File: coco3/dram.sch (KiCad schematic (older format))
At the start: 11 parts, among them CN4 Conn_01x12_Female, CN5 Conn_01x12_Female, CN6 Conn_01x12_Female, IC16 TMS4464, IC17 TMS4464, IC18 TMS4464, IC19 TMS4464

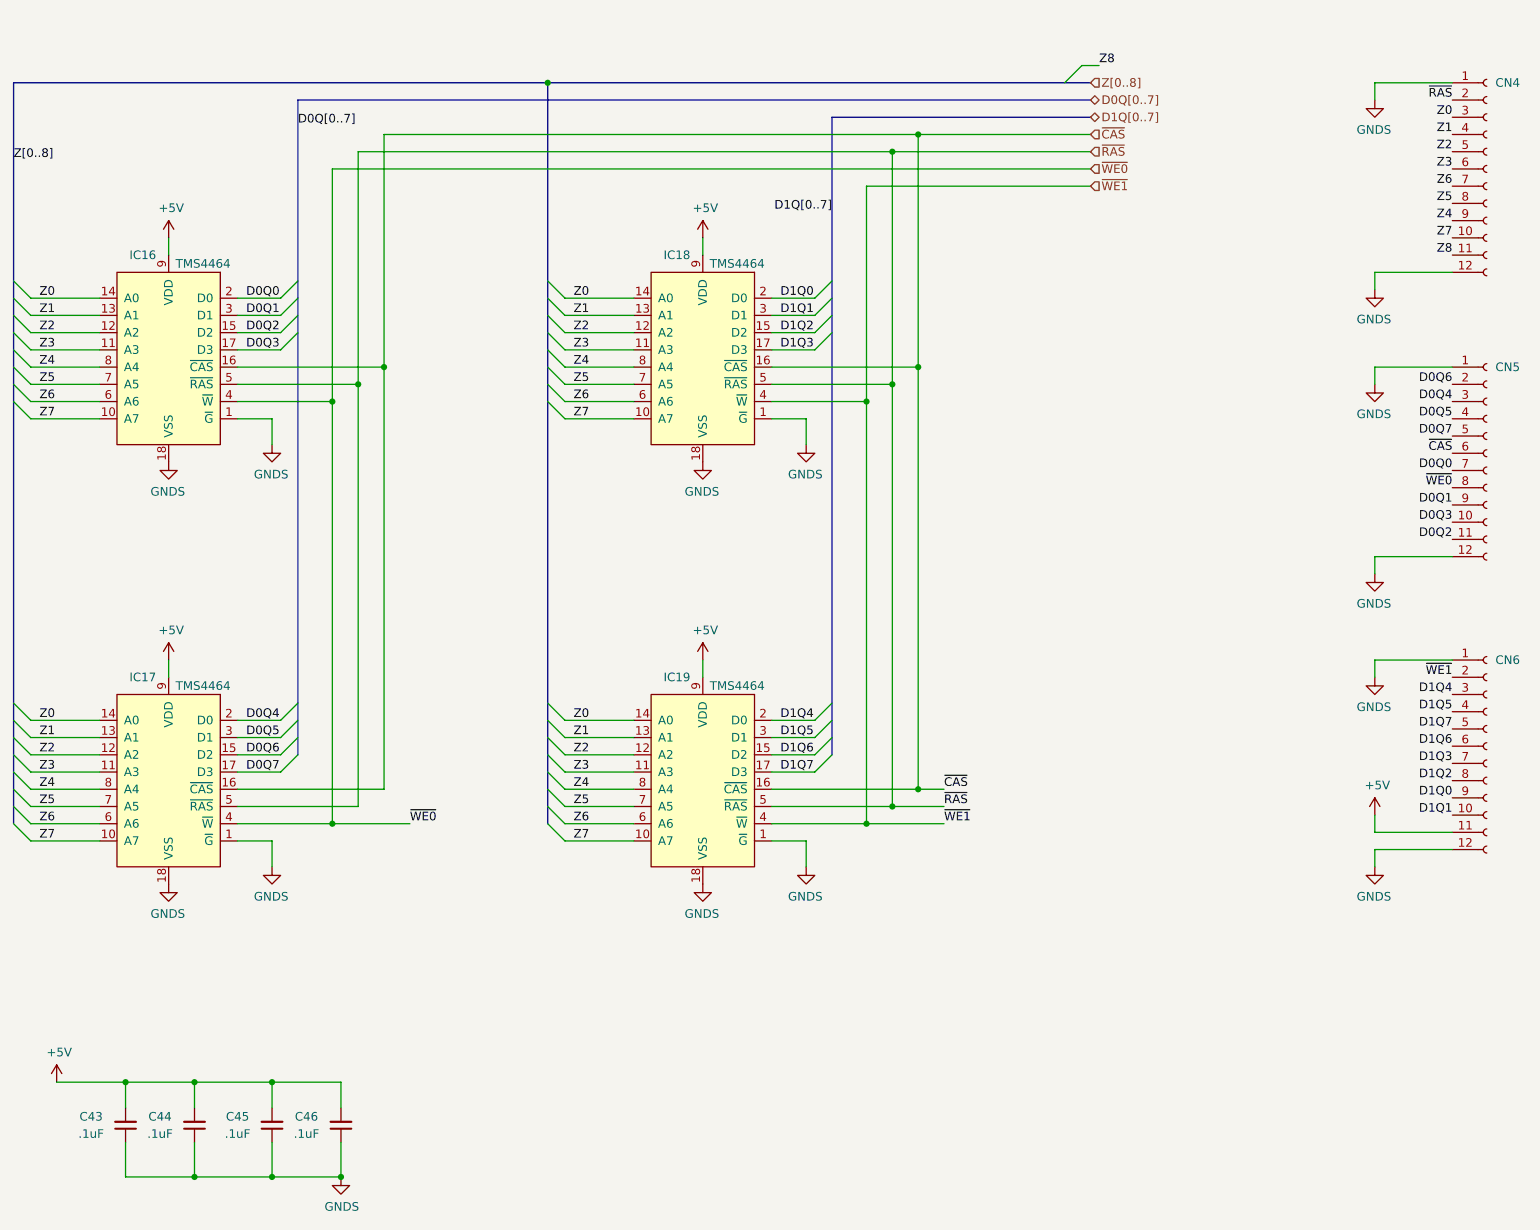
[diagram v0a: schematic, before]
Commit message: -replaced PIA's with he PLCC44 package versions -removed RF modulator -removed DRAM
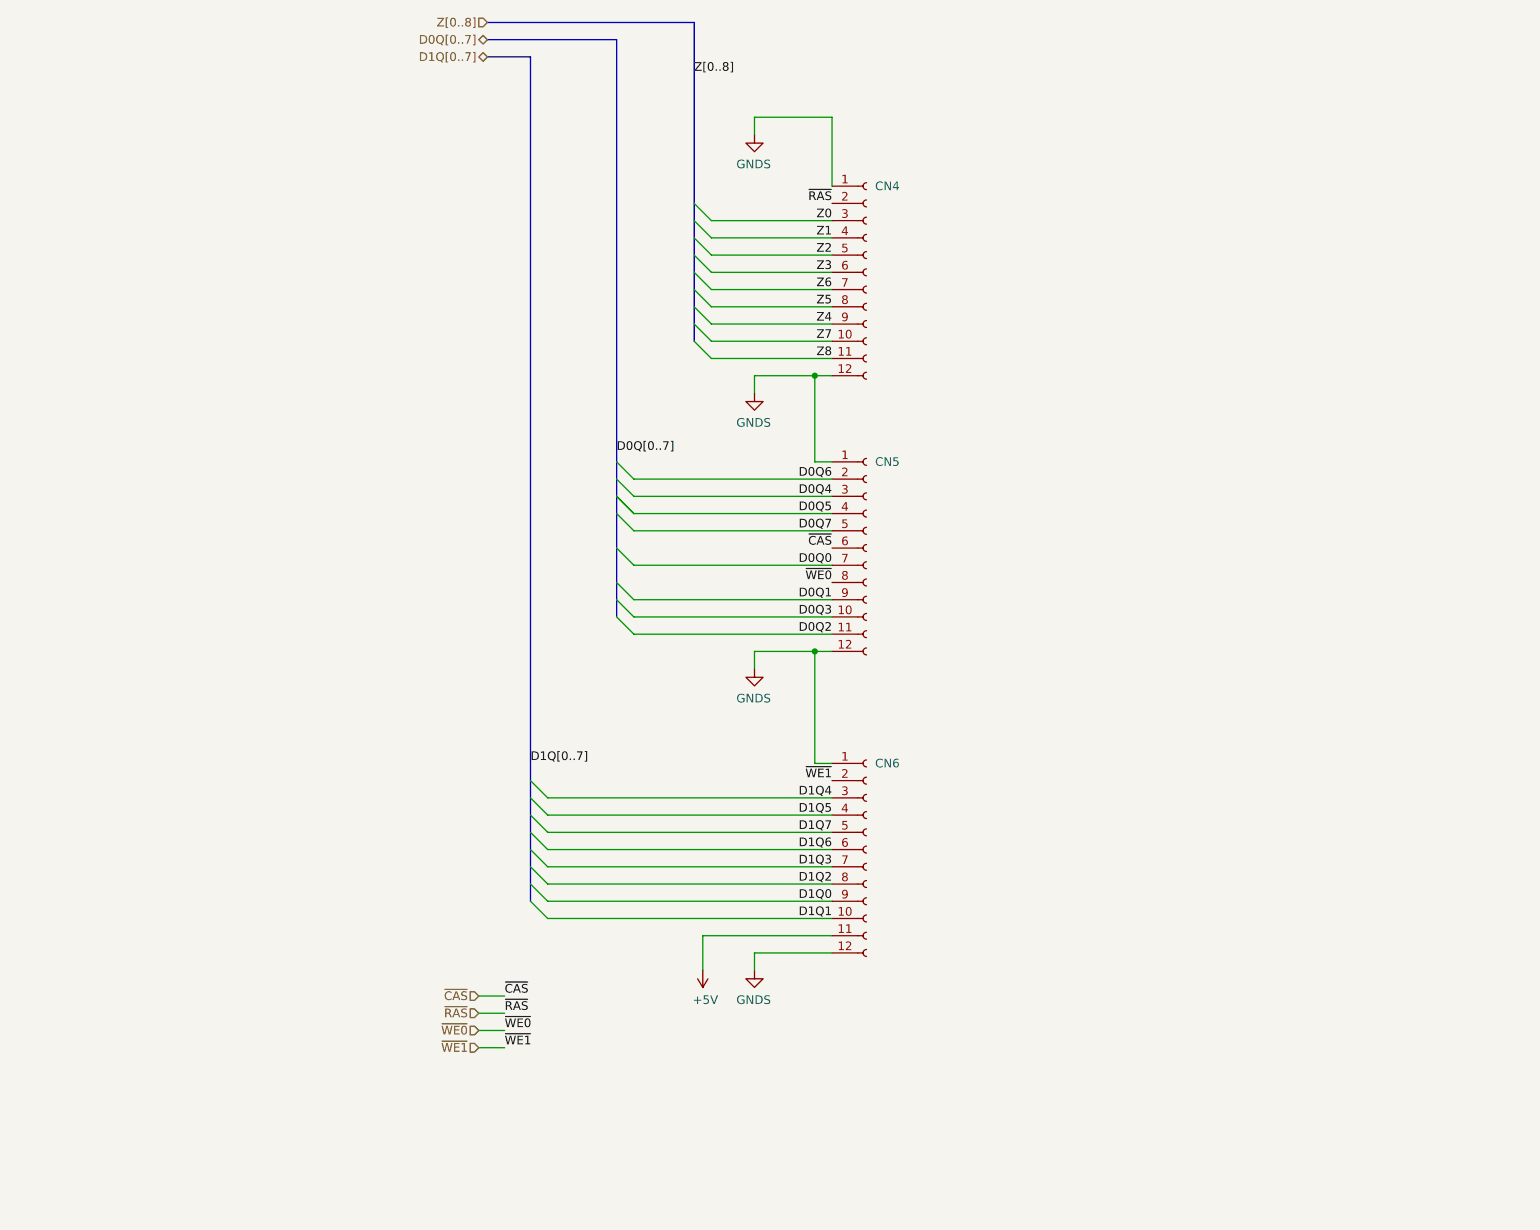
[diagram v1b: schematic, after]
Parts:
- removed C43, C44, C45, C46: .1uF, Capacitor_THT:C_Disc_D4.7mm_W2.5mm_P5.00mm, symbol Device:C_Small
- removed IC16, IC17, IC18, IC19: TMS4464, Package_DIP:DIP-18_W7.62mm_Socket, symbol Memory_RAM_Texas:TMS4464
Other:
- moved on the sheet: CN4, CN5, CN6

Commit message: routed the board
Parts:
- removed CN4, CN5, CN6: Conn_01x12_Female, coco2:PinSocket_1x12_P2.54mm_for_memory_board_adapter, symbol Connector:Conn_01x12_Female
- added CN4000: Conn_01x12_Female, Connector_PinSocket_2.54mm:PinSocket_1x12_P2.54mm_Vertical, symbol Connector:Conn_01x12_Female
- added CN56: Conn_01x24_Female, Connector_PinSocket_2.54mm:PinSocket_1x24_P2.54mm_Vertical, symbol Connector:Conn_01x24_Female
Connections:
- net +5V: now also CN56.23 (Pin_23)
- net D0Q0: now also CN56.7 (Pin_7)
- net D0Q1: now also CN56.9 (Pin_9)
- net D0Q2: now also CN56.11 (Pin_11)
- net D0Q3: now also CN56.10 (Pin_10)
- net D0Q4: now also CN56.3 (Pin_3)
- net D0Q5: now also CN56.4 (Pin_4)
- net D0Q6: now also CN56.2 (Pin_2)
- net D0Q7: now also CN56.5 (Pin_5)
- net D1Q0: now also CN56.21 (Pin_21)
- net D1Q1: now also CN56.22 (Pin_22)
- net D1Q2: now also CN56.20 (Pin_20)
- net D1Q3: now also CN56.19 (Pin_19)
- net D1Q4: now also CN56.15 (Pin_15)
- net D1Q5: now also CN56.16 (Pin_16)
- net D1Q6: now also CN56.18 (Pin_18)
- net D1Q7: now also CN56.17 (Pin_17)
- net GNDS: now also CN4000.1 (Pin_1), CN4000.12 (Pin_12), CN56.1 (Pin_1), CN56.12 (Pin_12), CN56.13 (Pin_13), CN56.24 (Pin_24)
- net Z0: now also CN4000.3 (Pin_3)
- net Z1: now also CN4000.4 (Pin_4)
- net Z2: now also CN4000.5 (Pin_5)
- net Z3: now also CN4000.6 (Pin_6)
- net Z4: now also CN4000.9 (Pin_9)
- net Z5: now also CN4000.8 (Pin_8)
- net Z6: now also CN4000.7 (Pin_7)
- net Z7: now also CN4000.10 (Pin_10)
- net Z8: now also CN4000.11 (Pin_11)
- net ~CAS: now also CN56.6 (Pin_6)
- net ~RAS: now also CN4000.2 (Pin_2)
- net ~WE0: now also CN56.8 (Pin_8)
- net ~WE1: now also CN56.14 (Pin_14)
